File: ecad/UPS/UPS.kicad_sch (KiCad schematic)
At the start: 0 parts

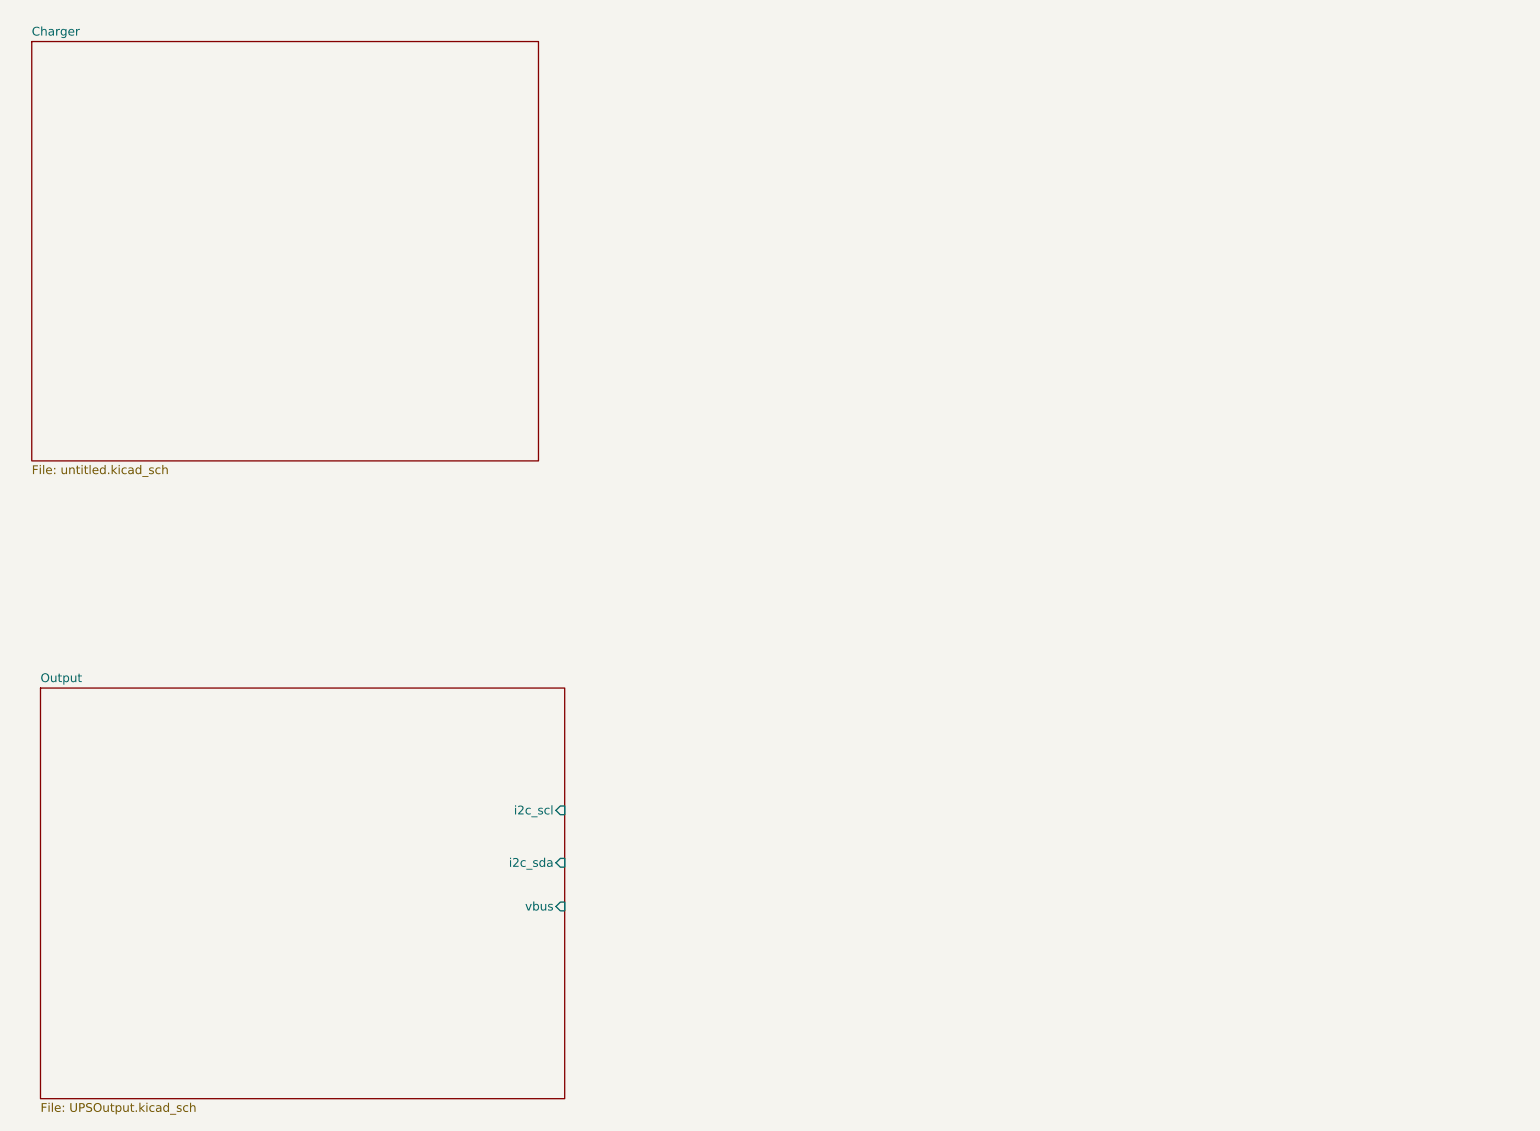
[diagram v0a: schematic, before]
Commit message: Did some routing, need to figure out how to route to BQ while appeasing DRC
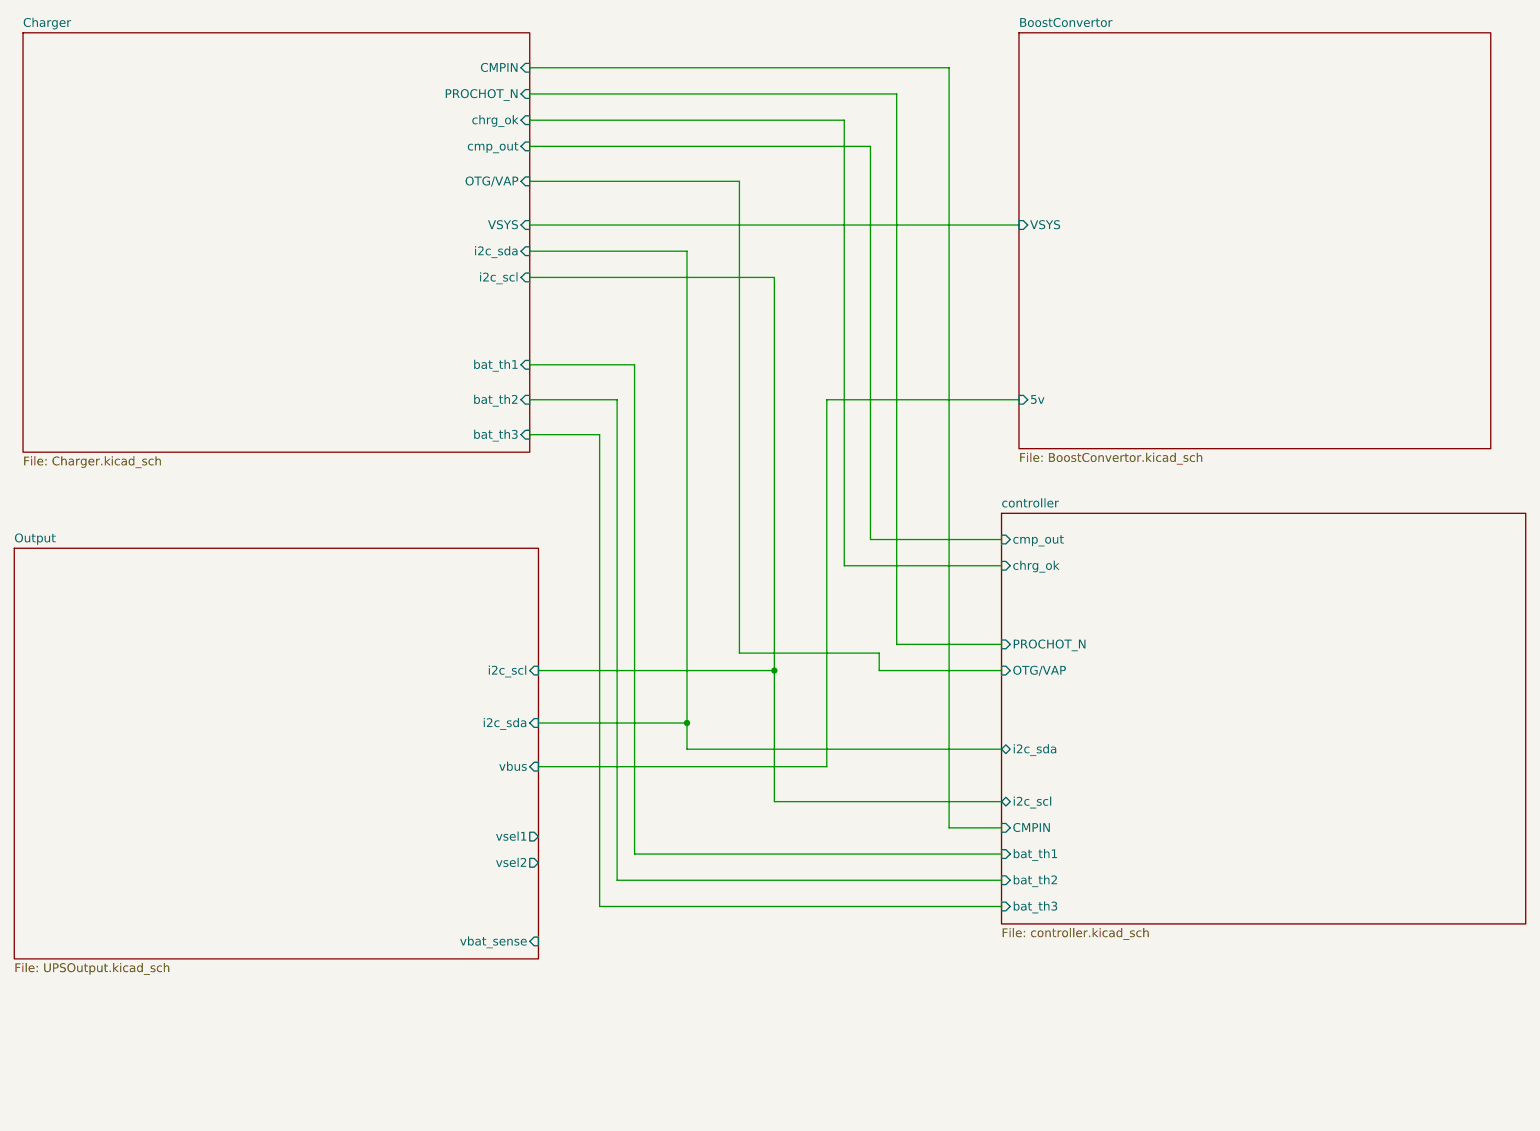
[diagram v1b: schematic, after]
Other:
- added sheet BoostConvertor (BoostConvertor.kicad_sch)
- added sheet controller (controller.kicad_sch)
- sheet Charger: file untitled.kicad_sch -> Charger.kicad_sch
- sheet Charger ports: added CMPIN, OTG/VAP, PROCHOT_N, VSYS, bat_th1, bat_th2, bat_th3, chrg_ok, cmp_out, i2c_scl, i2c_sda; removed none
- sheet Output ports: added vbat_sense, vsel1, vsel2; removed none
- company: (none) -> MTU Open Source Hardware Enterprise
- title: (none) -> UPS
